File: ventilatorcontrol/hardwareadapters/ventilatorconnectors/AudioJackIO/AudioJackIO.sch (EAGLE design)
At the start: 13 parts, among them X1 1503_11

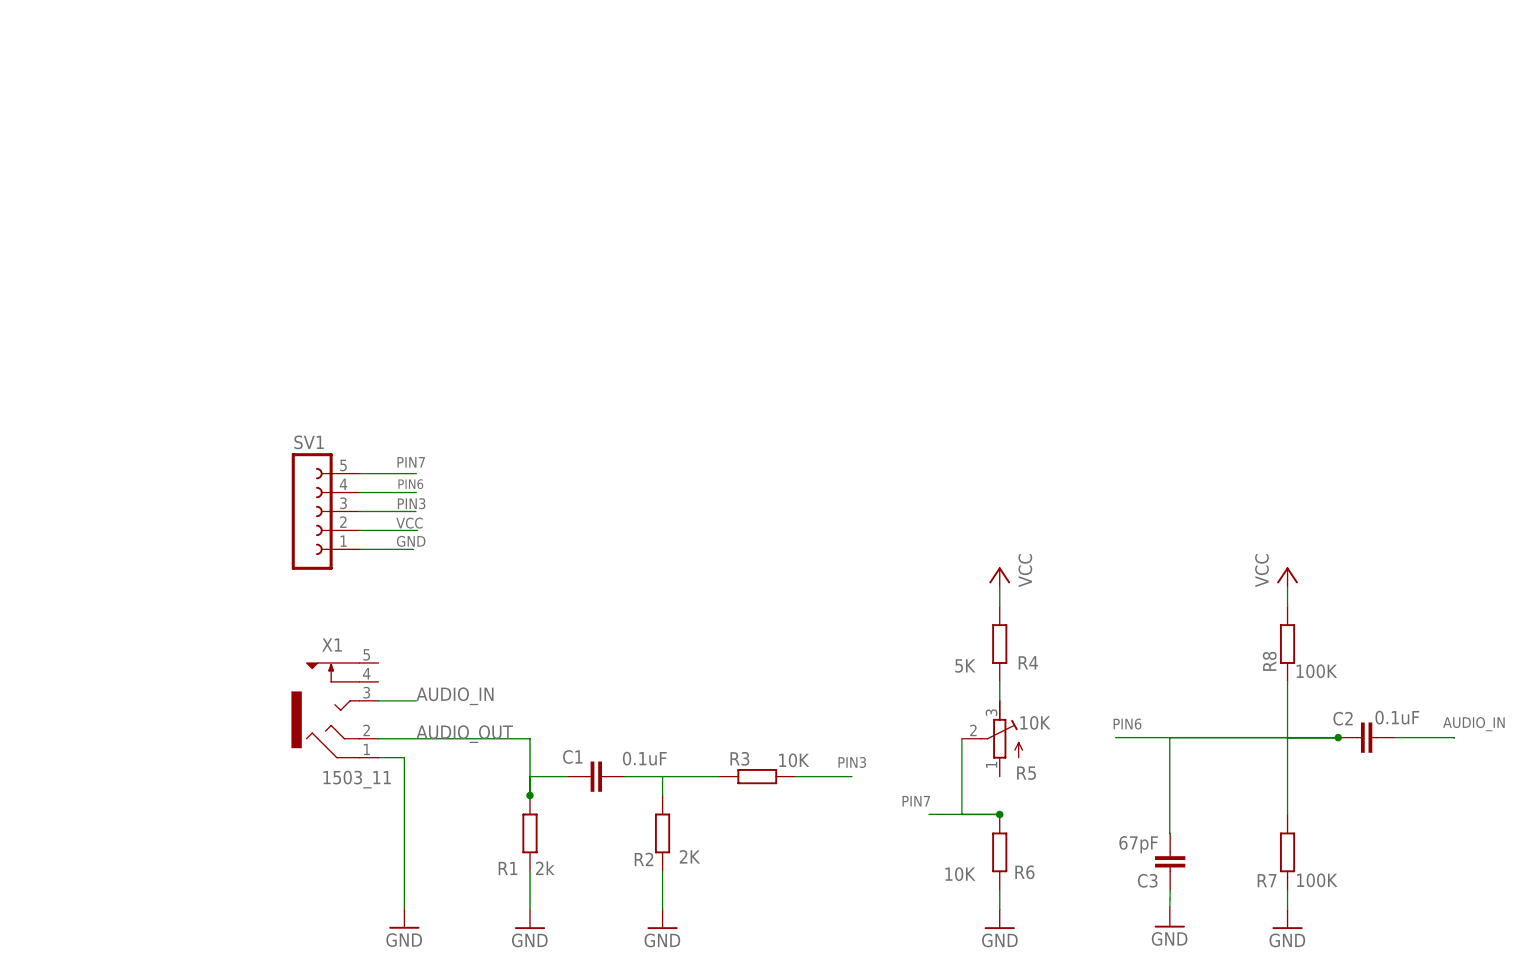
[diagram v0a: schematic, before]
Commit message: uController AudioJack interface schematic and layout. Added an alternative connector in parallel to the audio jack and gerber file exported for a small and standard arduino shield.
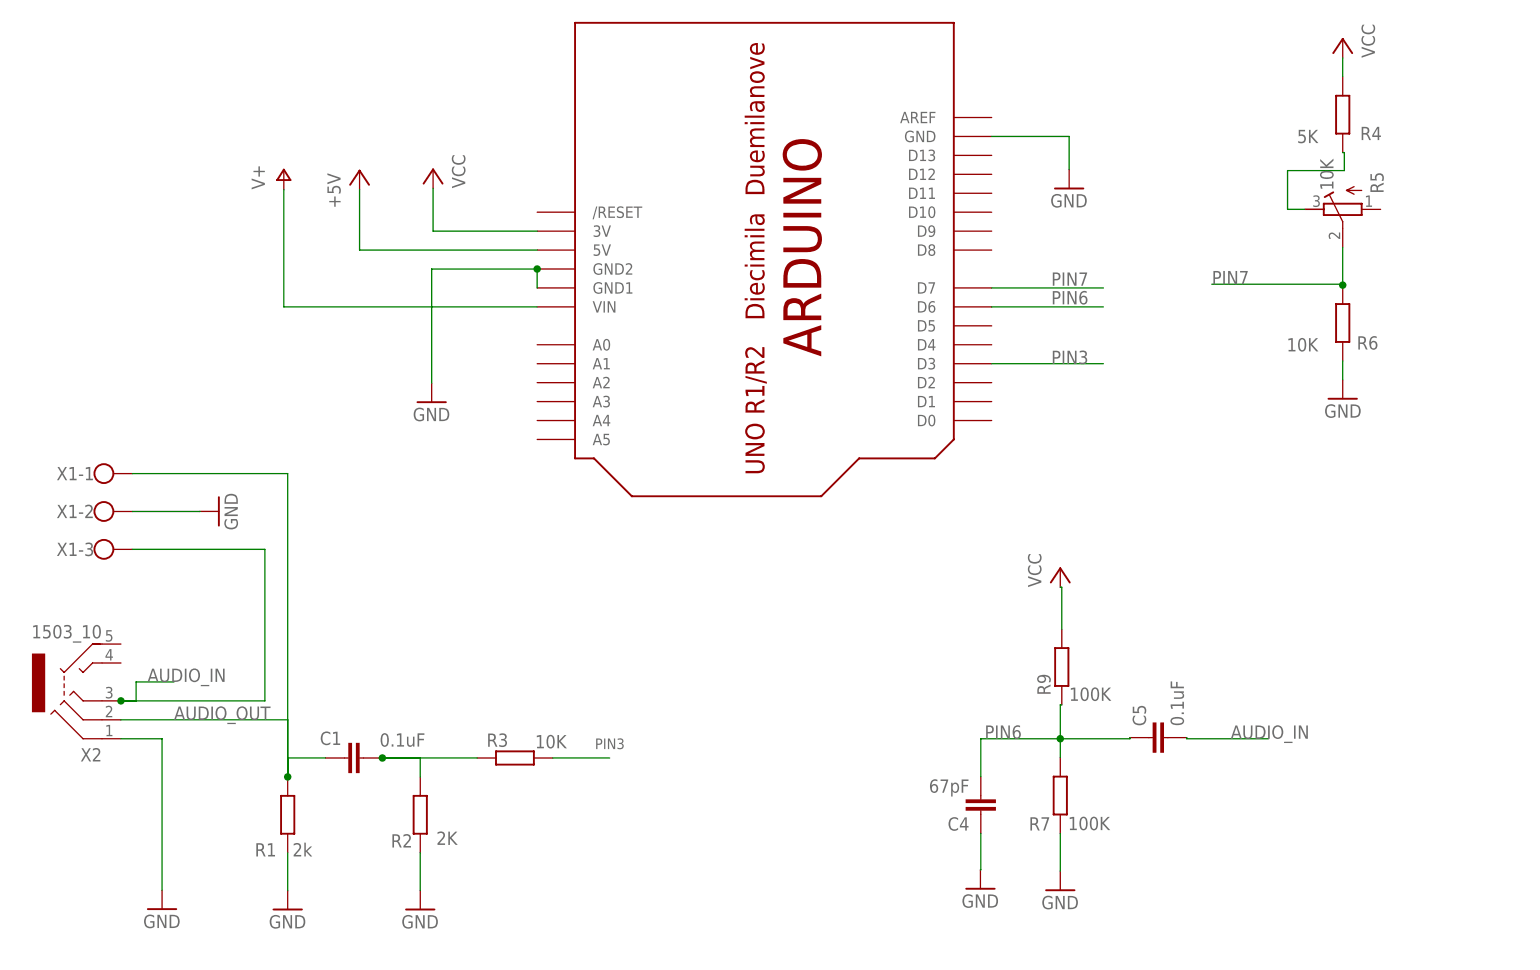
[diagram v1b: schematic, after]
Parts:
- removed C2: 0.1uF, rcl:C-EU025-025X050
- removed C3: 67pF, rcl:C-EU025-025X050
- removed R8: 100K, rcl:R-EU_0204/7
- removed SV1: (no value), con-lsta:FE05-1
- added C4: 67pF, rcl:C-EU025-025X050
- added C5: 0.1uF, rcl:C-EU025-025X050
- added R9: 100K, rcl:R-EU_0204/7
- added U$1: ARDUINO-BPLACE, adafruit:ARDUINO-BPLACE
- added X2: 1503_10, con-lumberg:1503_10
- X1: value 1503_11 -> (none); device con-lumberg:1503_11 -> con-wago-500:W237-103
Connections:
- new net +5V: U$1.5V
- new net V+: U$1.VIN
- net AUDIO_IN: now also C5.2, X1-3.KL, X2.3; no longer C2.2, X1.3
- net AUDIO_OUT: now also X1-1.KL, X2.2; no longer X1.2
- net GND: now also C4.1, U$1.GND, U$1.GND1, U$1.GND2, X1-2.KL, X2.1; no longer C3.1, SV1.1, X1.1
- net PIN3: now also U$1.D3; no longer SV1.3
- net PIN6: now also C4.2, C5.1, R9.1, U$1.D6; no longer C2.1, C3.2, R8.1, SV1.4
- net PIN7: now also U$1.D7; no longer SV1.5
- net VCC: now also R9.2, U$1.3V; no longer R8.2, SV1.2
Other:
- note added: "Audio Jack Connector"
- moved on the sheet: C1, R1, R2, R3, R4, R5, R6, R7
